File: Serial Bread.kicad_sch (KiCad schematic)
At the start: 20 parts, among them J1 TYPE-C-31-M-12, J2 Conn_02x04_Top_Bottom, U1 CH340C, U2 AP2112K-3.3

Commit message: Initial commit R1.1
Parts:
- removed J1: TYPE-C-31-M-12, SnapEDA Library:HRO_TYPE-C-31-M-12, symbol TYPE-C-31-M-12:TYPE-C-31-M-12
- removed JP1: Jumper_3_Open, Connector_PinHeader_1.27mm:PinHeader_1x03_P1.27mm_Vertical, symbol Jumper:Jumper_3_Open
- added D3: LED RED, LED_SMD:LED_0603_1608Metric, symbol Device:LED
- added J1: USB_C_Receptacle_USB2.0, Connector_USB:USB_C_Receptacle_HRO_TYPE-C-31-M-12, symbol Connector:USB_C_Receptacle_USB2.0
- added R5: 1k, Resistor_SMD:R_0402_1005Metric, symbol Device:R
- added SW1: SW_SPDT, Custom_Switches:CL-SB-12B-02T, symbol Switch:SW_SPDT
- C1, C2: footprint Capacitor_SMD:C_0603_1608Metric -> Capacitor_SMD:C_0402_1005Metric; MPN C14663 -> C1525
- C3: footprint Capacitor_SMD:C_0603_1608Metric -> Capacitor_SMD:C_0402_1005Metric; MPN C19702 -> C15525
- C4, C5: footprint Capacitor_SMD:C_0603_1608Metric -> Capacitor_SMD:C_0402_1005Metric; MPN C15849 -> C52923
- J2: MPN C2833740 -> C358726
- R1, R2: footprint Resistor_SMD:R_0603_1608Metric -> Resistor_SMD:R_0402_1005Metric; MPN C23186 -> C25905
- R3, R4: footprint Resistor_SMD:R_0603_1608Metric -> Resistor_SMD:R_0402_1005Metric; MPN C21190 -> C11702
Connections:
- net +3.3V: now also R5.1, SW1.1 (A)
- net +5V: now also J1.A4 (VBUS), J1.A9 (VBUS), J1.B4 (VBUS), J1.B9 (VBUS), SW1.3 (C)
- net CC1: now also J1.A5 (CC1)
- net CC2: now also J1.B5 (CC2)
- net D+: now also J1.A6 (D+), J1.B6 (D+)
- net D-: now also J1.A7 (D-), J1.B7 (D-)
- net GND: now also D3.1 (K), J1.A1 (GND), J1.A12 (GND), J1.B1 (GND), J1.B12 (GND)
- net SHLD: now also J1.S1 (SHIELD)
- net VCC: now also SW1.2 (B)
- new net: D3.2 (A), R5.2
- no-connect marks 7 -> 8
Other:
- note added: "CL-SB-12B-02T"
- moved on the sheet: D2, R4

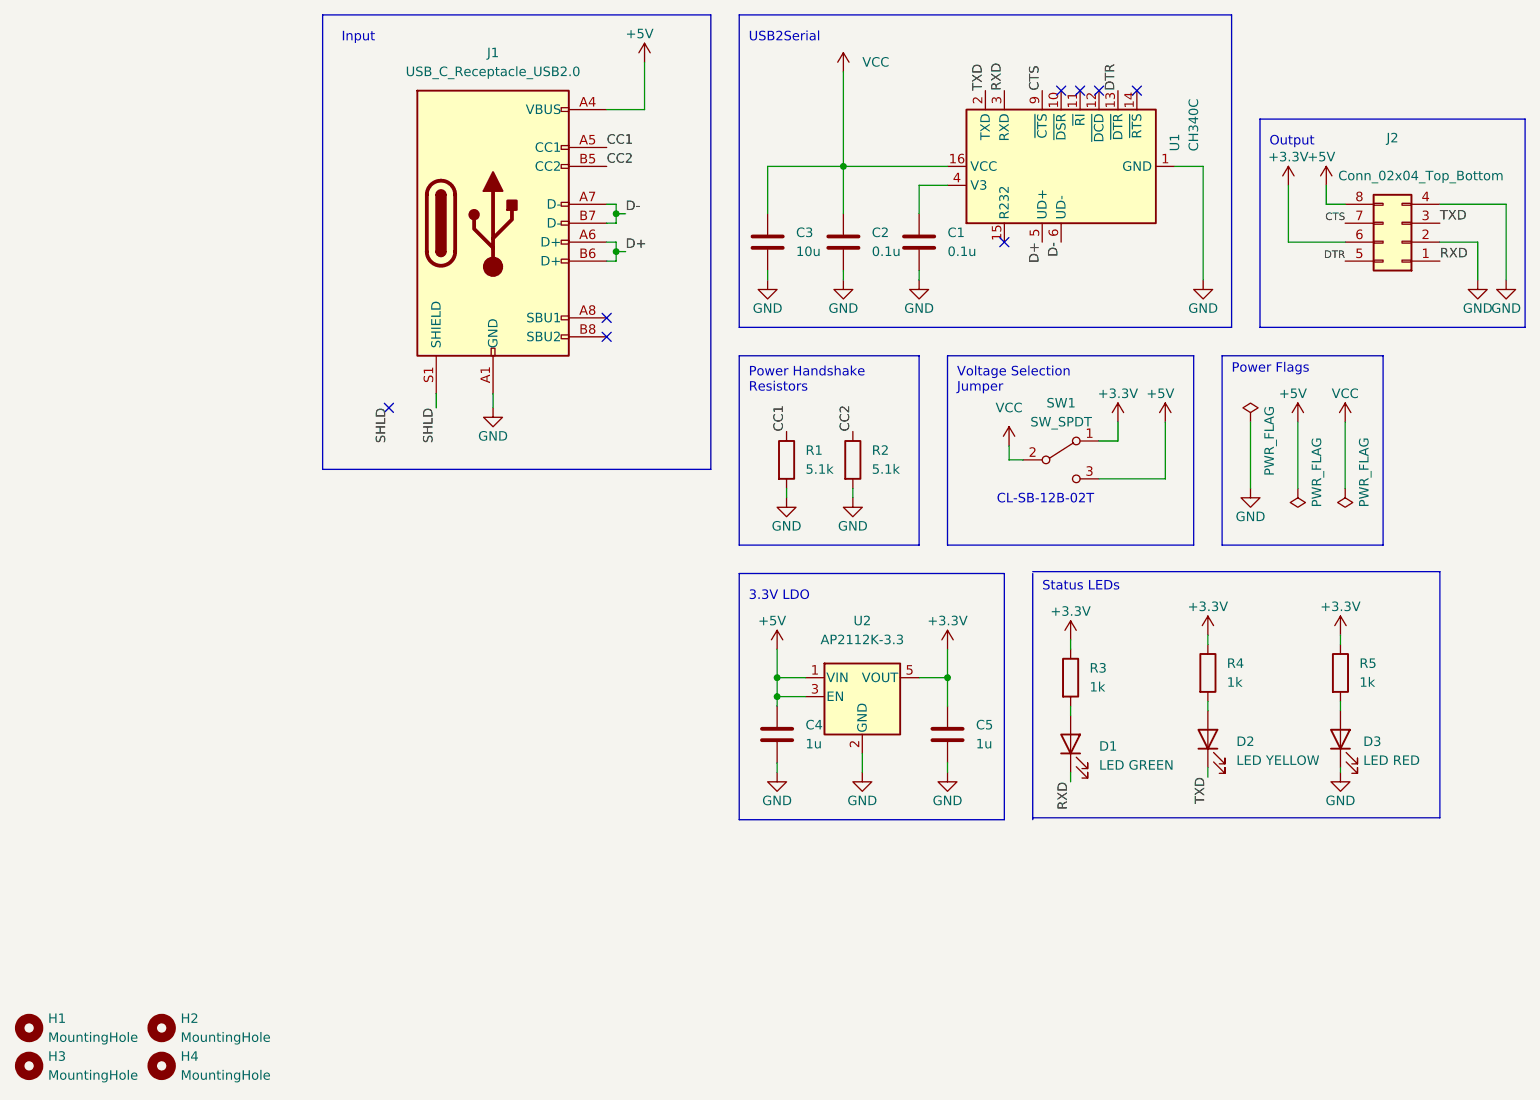
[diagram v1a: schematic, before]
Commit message: Revert "Initial commit R1.1"
This reverts commit dbca94149cb8df2c718ea664c1760d3caefabc82.
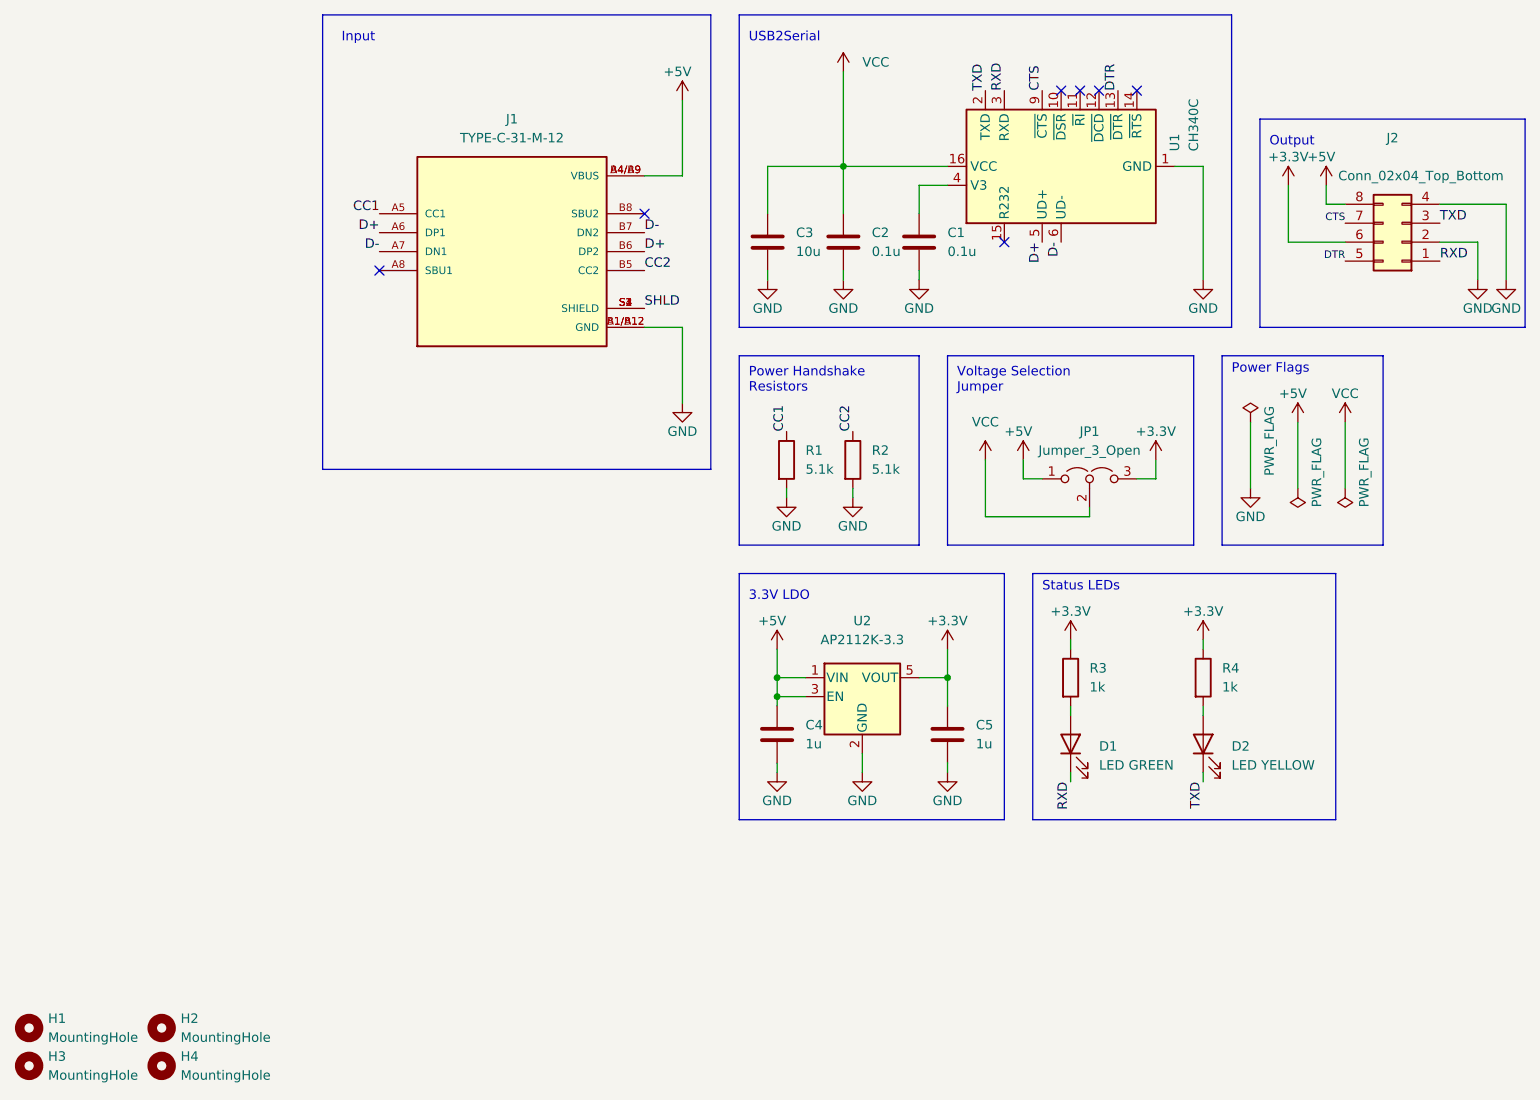
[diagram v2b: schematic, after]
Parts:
- removed D3: LED RED, LED_SMD:LED_0603_1608Metric, symbol Device:LED
- removed J1: USB_C_Receptacle_USB2.0, Connector_USB:USB_C_Receptacle_HRO_TYPE-C-31-M-12, symbol Connector:USB_C_Receptacle_USB2.0
- removed R5: 1k, Resistor_SMD:R_0402_1005Metric, symbol Device:R
- removed SW1: SW_SPDT, Custom_Switches:CL-SB-12B-02T, symbol Switch:SW_SPDT
- added J1: TYPE-C-31-M-12, SnapEDA Library:HRO_TYPE-C-31-M-12, symbol TYPE-C-31-M-12:TYPE-C-31-M-12
- added JP1: Jumper_3_Open, Connector_PinHeader_1.27mm:PinHeader_1x03_P1.27mm_Vertical, symbol Jumper:Jumper_3_Open
- C1, C2: footprint Capacitor_SMD:C_0402_1005Metric -> Capacitor_SMD:C_0603_1608Metric; MPN C1525 -> C14663
- C3: footprint Capacitor_SMD:C_0402_1005Metric -> Capacitor_SMD:C_0603_1608Metric; MPN C15525 -> C19702
- C4, C5: footprint Capacitor_SMD:C_0402_1005Metric -> Capacitor_SMD:C_0603_1608Metric; MPN C52923 -> C15849
- J2: MPN C358726 -> C2833740
- R1, R2: footprint Resistor_SMD:R_0402_1005Metric -> Resistor_SMD:R_0603_1608Metric; MPN C25905 -> C23186
- R3, R4: footprint Resistor_SMD:R_0402_1005Metric -> Resistor_SMD:R_0603_1608Metric; MPN C11702 -> C21190
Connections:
- net +3.3V: now also JP1.3 (B)
- net +5V: now also J1.A4/B9 (VBUS), J1.B4/A9 (VBUS), JP1.1 (A)
- net CC1: now also J1.A5 (CC1)
- net CC2: now also J1.B5 (CC2)
- net D+: now also J1.A6 (DP1), J1.B6 (DP2)
- net D-: now also J1.A7 (DN1), J1.B7 (DN2)
- net GND: now also J1.A1/B12 (GND), J1.B1/A12 (GND)
- net SHLD: now also J1.S1 (SHIELD), J1.S2 (SHIELD), J1.S3 (SHIELD), J1.S4 (SHIELD)
- net VCC: now also JP1.2 (C)
- no-connect marks 8 -> 7
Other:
- note removed: "CL-SB-12B-02T"
- moved on the sheet: D2, R4
